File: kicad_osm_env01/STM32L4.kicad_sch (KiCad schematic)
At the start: 27 parts

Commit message: added stml433 to schematic and carried out some mods
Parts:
- added C? (x2): 100nF, Capacitor_SMD:C_0402_1005Metric, symbol device:C
- added C? (x2): 1uF, Capacitor_SMD:C_0402_1005Metric, symbol device:C
- added L?: 2A/0.05DCR, Inductor_SMD:L_0402_1005Metric, symbol device:Ferrite_Bead
- added R?: 0R, symbol device:R
- added U?: STM32L433VCTx, LQFP100, symbol Devtank:STM32L433VCTx
- C1, C12: value (none) -> 10pF; footprint (none) -> Capacitor_SMD:C_0402_1005Metric
- C13, C27: value (none) -> DNF; footprint (none) -> Capacitor_SMD:C_0402_1005Metric
- C28, C29, C30, C44, C51, C62: renamed from C?; value (none) -> 100nF; footprint (none) -> Capacitor_SMD:C_0402_1005Metric
- C59: renamed from C?; value (none) -> 4.7uF; footprint (none) -> Capacitor_SMD:C_0603_1608Metric
- C60: renamed from C?; value (none) -> 1uF; footprint (none) -> Capacitor_SMD:C_0402_1005Metric
- C61: renamed from C?; value (none) -> 10nF; footprint (none) -> Capacitor_SMD:C_0402_1005Metric
- D8: value (none) -> RED; footprint (none) -> Devtank_PCB_lib:LED_Rectangular_W4.5mm_H7.3mm_Horizontal_2.54mm_Z3.0mm
- J5: value (none) -> Conn_02x03_Odd_Even; footprint (none) -> Connector:Tag-Connect_TC2030-IDC-NL_2x03_P1.27mm_Vertical
- L2: renamed from L?; value (none) -> 2A/0.05DCR; footprint (none) -> Inductor_SMD:L_0402_1005Metric
- R119, R16: value (none) -> 10k; footprint (none) -> Resistor_SMD:R_0603_1608Metric
- R15, R30: value (none) -> DNF; footprint (none) -> Resistor_SMD:R_0603_1608Metric
- R26: value (none) -> 390R; footprint (none) -> Resistor_SMD:R_0603_1608Metric
- R37: value (none) -> 0R; footprint (none) -> Resistor_SMD:R_0603_1608Metric
- R6: value (none) -> 1.3k; footprint (none) -> Resistor_SMD:R_0603_1608Metric
- S1: value (none) -> B3U-1100P; footprint (none) -> Button_Switch_SMD:SW_SPST_B3U-1100P
- U14: value (none) -> STM32L451RCTx; footprint (none) -> Package_QFP:LQFP-64_10x10mm_P0.5mm
- Y1: value (none) -> 8MHZ; footprint (none) -> Crystal:Crystal_SMD_Abracon_ABM3C-4Pin_5.0x3.2mm
- Y2: value (none) -> DNF; footprint (none) -> Crystal:Crystal_SMD_7050-4Pin_7.0x5.0mm
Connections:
- net +3V3: now also C?.1, C?.1, L?.2, U?.100 (VDD), U?.11 (VDD), U?.28 (VDD), U?.50 (VDD), U?.73 (VDDUSB), U?.75 (VDD)
- net 32.768KHZ_crystal_out: now also U?.9 (ADC1_EXTI15/ADC2_EXTI15/ADC3_EXTI15/RCC_OSC32_OUT/PC15)
- net 3V3A_STM: now also U?.22 (VDDA)
- net 8MHZ_crystal_in: now also U?.12 (PH0/RCC_OSC_IN)
- net 8MHZ_crystal_out: now also U?.13 (PH1/RCC_OSC_OUT)
- net ADC2: now also U?.24 (ADC1_IN6/ADC2_IN6/LCD_SEG0/OPAMP1_VINM/TIM15_CH1N/TIM2_CH2/TIM5_CH2/UART4_RX/USART2_DE/USART2_RTS/PA1)
- net ADC3: now also U?.17 (ADC1_IN3/ADC2_IN3/ADC3_IN3/DFSDM_CKOUT/LCD_SEG20/LPTIM1_IN2/SPI2_MISO/PC2)
- net ADC4: now also U?.18 (ADC1_IN4/ADC2_IN4/ADC3_IN4/LCD_VLCD/LPTIM1_ETR/LPTIM2_ETR/SAI1_SD_A/SPI2_MOSI/PC3)
- net ADC5: now also U?.35 (ADC1_IN15/ADC2_IN15/COMP1_OUT/LCD_SEG5/OPAMP2_VOUT/QUADSPI_BK1_IO1/TIM1_CH2N/TIM3_CH3/TIM8_CH2N/USART3_CK/PB0)
- net ADC6: now also U?.36 (ADC1_IN16/ADC2_IN16/COMP1_INM/DFSDM_DATIN0/LCD_SEG6/LPTIM2_IN1/QUADSPI_BK1_IO0/TIM1_CH3N/TIM3_CH4/TIM8_CH3N/USART3_DE/USART3_RTS/PB1)
- net ADC7: now also U?.15 (ADC1_IN1/ADC2_IN1/ADC3_IN1/DFSDM_DATIN4/I2C3_SCL/LCD_SEG18/LPTIM1_IN1/LPTIM2_IN1/LPUART1_RX/PC0)
- net ADC8: now also U14.20 (ADC1_IN9/ADC2_IN9/DAC1_OUT1/LPTIM2_OUT/SAI1_FS_B/SPI1_NSS/SPI3_NSS/USART2_CK/PA4), U?.29 (ADC1_IN9/ADC2_IN9/DAC1_OUT1/LPTIM2_OUT/SAI1_FS_B/SPI1_NSS/SPI3_NSS/USART2_CK/PA4); no longer U14.9 (PC1/ADC1_IN2/ADC2_IN2/ADC3_IN2/DFSDM_CKIN4/I2C3_SDA/LCD_SEG19/LPTIM1_OUT/LPUART1_TX)
- net BOOT0: now also U?.94 (BOOT0)
- net CAN1_RX: now also U?.51 (DFSDM_DATIN1/I2C2_SMBA/LCD_SEG12/LPUART1_DE/LPUART1_RTS/SAI2_FS_A/SPI2_NSS/SWPMI1_IO/TIM15_BKIN/TIM1_BKIN/TIM1_BKIN_COMP2/TSC_G1_IO1/USART3_CK/PB12)
- net CAN1_TX: now also U?.52 (DFSDM_CKIN1/I2C2_SCL/LCD_SEG13/LPUART1_CTS/SAI2_SCK_A/SPI2_SCK/SWPMI1_TX/TIM15_CH1N/TIM1_CH1N/TSC_G1_IO2/USART3_CTS/PB13)
- net GND: now also C?.2, C?.2, C?.2, C?.2, U?.10 (VSS), U?.19 (VSSA), U?.20 (VREF-), U?.27 (VSS), U?.49 (VSS), U?.74 (VSS), U?.99 (VSS)
- net GPIO1: now also U?.63 (DFSDM_CKIN3/LCD_SEG24/SAI2_MCLK_A/SDMMC1_D6/TIM3_CH1/TIM8_CH1/TSC_G4_IO1/PC6)
- net GPIO10: now also U?.77 (ADC1_EXTI15/ADC2_EXTI15/ADC3_EXTI15/LCD_SEG17/SAI2_FS_B/SPI1_NSS/SPI3_NSS/SYS_JTDI/TIM2_CH1/TIM2_ETR/TSC_G3_IO1/UART4_DE/UART4_RTS/PA15)
- net GPIO11: now also U?.64 (DFSDM_DATIN3/LCD_SEG25/SAI2_MCLK_B/SDMMC1_D7/TIM3_CH2/TIM8_CH2/TSC_G4_IO2/PC7)
- net GPIO12: now also U?.90 (COMP2_INP/LCD_SEG8/SAI1_MCLK_B/SPI1_MISO/SPI3_MISO/SYS_JTRST/TIM17_BKIN/TIM3_CH1/TSC_G2_IO1/UART5_DE/UART5_RTS/USART1_CTS/PB4)
- net GPIO13: now also U?.91 (COMP2_OUT/I2C1_SMBA/LCD_SEG9/LPTIM1_IN1/SAI1_SD_B/SPI1_MOSI/SPI3_MOSI/TIM16_BKIN/TIM3_CH2/TSC_G2_IO2/UART5_CTS/USART1_CK/PB5)
- net GPIO14: now also U?.53 (DFSDM_DATIN2/I2C2_SDA/LCD_SEG14/SAI2_MCLK_A/SPI2_MISO/SWPMI1_RX/TIM15_CH1/TIM1_CH2N/TIM8_CH2N/TSC_G1_IO3/USART3_DE/USART3_RTS/PB14)
- net GPIO15: now also U?.54 (ADC1_EXTI15/ADC2_EXTI15/ADC3_EXTI15/DFSDM_CKIN2/LCD_SEG15/RTC_REFIN/SAI2_SD_A/SPI2_MOSI/SWPMI1_SUSPEND/TIM15_CH2/TIM1_CH3N/TIM8_CH3N/TSC_G1_IO4/PB15)
- net GPIO16: now also U?.83 (PD2/LCD_COM7/LCD_SEG31/LCD_SEG43/SDMMC1_CMD/TIM3_ETR/TSC_SYNC/UART5_RX/USART3_DE/USART3_RTS)
- net GPIO2: now also U?.65 (LCD_SEG26/SDMMC1_D0/TIM3_CH3/TIM8_CH3/TSC_G4_IO3/PC8)
- net GPIO3: now also U?.37 (COMP1_INP/DFSDM_CKIN0/I2C3_SMBA/LPTIM1_OUT/RTC_OUT_ALARM/RTC_OUT_CALIB/PB2)
- net GPIO4: now also U?.66 (DAC1_EXTI9/LCD_SEG27/SAI2_EXTCLK/SDMMC1_D1/TIM3_CH4/TIM8_BKIN2/TIM8_BKIN2_COMP1/TIM8_CH4/TSC_G4_IO4/USB_OTG_FS_NOE/PC9)
- net GPIO6: now also U?.89 (COMP2_INM/LCD_SEG7/SAI1_SCK_B/SPI1_SCK/SPI3_SCK/SYS_JTDO-SWO/TIM2_CH2/USART1_DE/USART1_RTS/PB3)
- net GPIO7: now also U?.80 (LCD_COM6/LCD_SEG30/LCD_SEG42/SAI2_SD_B/SDMMC1_CK/SPI3_MOSI/TSC_G3_IO4/UART5_TX/USART3_CK/PC12)
- net GPIO8: now also U?.70 (ADC1_EXTI11/ADC2_EXTI11/ADC3_EXTI11/CAN1_RX/TIM1_BKIN2/TIM1_BKIN2_COMP1/TIM1_CH4/USART1_CTS/USB_OTG_FS_DM/PA11)
- net GPIO9: now also U?.71 (CAN1_TX/TIM1_ETR/USART1_DE/USART1_RTS/USB_OTG_FS_DP/PA12)
- net I2C1_SCL: now also U?.95 (CAN1_RX/DFSDM_DATIN6/I2C1_SCL/LCD_SEG16/SAI1_MCLK_A/SDMMC1_D4/TIM16_CH1/TIM4_CH3/PB8)
- net I2C1_SDA: now also U?.96 (CAN1_TX/DAC1_EXTI9/DFSDM_CKIN6/I2C1_SDA/IR_OUT/LCD_COM3/SAI1_FS_A/SDMMC1_D5/SPI2_NSS/TIM17_CH1/TIM4_CH4/PB9)
- net LPUART1_RX: now also U?.47 (COMP1_OUT/DFSDM_DATIN7/I2C2_SCL/LCD_SEG10/LPUART1_RX/QUADSPI_CLK/SAI1_SCK_A/SPI2_SCK/TIM2_CH3/USART3_TX/PB10)
- net LPUART1_TX: now also U?.48 (ADC1_EXTI11/ADC2_EXTI11/ADC3_EXTI11/COMP2_OUT/DFSDM_CKIN7/I2C2_SDA/LCD_SEG11/LPUART1_TX/QUADSPI_NCS/TIM2_CH4/USART3_RX/PB11)
- net SAI1_FS_A: now also U?.68 (DAC1_EXTI9/LCD_COM1/TIM15_BKIN/TIM1_CH2/USART1_TX/USB_OTG_FS_VBUS/PA9)
- net SAI1_SCK_A: now also U?.67 (LCD_COM0/LPTIM2_OUT/RCC_MCO/TIM1_CH1/USART1_CK/USB_OTG_FS_SOF/PA8)
- net SAI1_SD_A: now also U?.69 (LCD_COM2/TIM17_BKIN/TIM1_CH3/USART1_RX/USB_OTG_FS_ID/PA10)
- net SPI1_CS: now also U14.9 (PC1/ADC1_IN2/ADC2_IN2/ADC3_IN2/DFSDM_CKIN4/I2C3_SDA/LCD_SEG19/LPTIM1_OUT/LPUART1_TX), U?.16 (ADC1_IN2/ADC2_IN2/ADC3_IN2/DFSDM_CKIN4/I2C3_SDA/LCD_SEG19/LPTIM1_OUT/LPUART1_TX/PC1); no longer U14.20 (ADC1_IN9/ADC2_IN9/DAC1_OUT1/LPTIM2_OUT/SAI1_FS_B/SPI1_NSS/SPI3_NSS/USART2_CK/PA4)
- net SPI1_MISO: now also U?.31 (ADC1_IN11/ADC2_IN11/LCD_SEG3/OPAMP2_VINP/QUADSPI_BK1_IO3/SPI1_MISO/TIM16_CH1/TIM1_BKIN/TIM1_BKIN_COMP2/TIM3_CH1/TIM8_BKIN/TIM8_BKIN_COMP2/USART3_CTS/PA6)
- net SPI1_MOSI: now also U?.32 (ADC1_IN12/ADC2_IN12/LCD_SEG4/OPAMP2_VINM/QUADSPI_BK1_IO2/SPI1_MOSI/TIM17_CH1/TIM1_CH1N/TIM3_CH2/TIM8_CH1N/PA7)
- net SPI1_SCK: now also U?.30 (ADC1_IN10/ADC2_IN10/DAC1_OUT2/LPTIM2_ETR/SPI1_SCK/TIM2_CH1/TIM2_ETR/TIM8_CH1N/PA5)
- net STM_NRST: now also U?.14 (NRST)
- net SWCLK: now also U?.76 (SYS_JTCK-SWCLK/PA14)
- net SWD_IO: now also U?.72 (IR_OUT/SYS_JTMS-SWDIO/USB_OTG_FS_NOE/PA13)
- net UART4_RX: now also U?.79 (ADC1_EXTI11/ADC2_EXTI11/ADC3_EXTI11/LCD_COM5/LCD_SEG29/LCD_SEG41/SAI2_MCLK_B/SDMMC1_D3/SPI3_MISO/TSC_G3_IO3/UART4_RX/USART3_RX/PC11)
- net UART4_TX: now also U?.78 (LCD_COM4/LCD_SEG28/LCD_SEG40/SAI2_SCK_B/SDMMC1_D2/SPI3_SCK/TSC_G3_IO2/UART4_TX/USART3_TX/PC10)
- net USART1_RX: now also U?.93 (COMP2_INM/DFSDM_CKIN5/FMC_NL/I2C1_SDA/LCD_SEG21/LPTIM1_IN2/SYS_PVD_IN/TIM17_CH1N/TIM4_CH2/TIM8_BKIN/TIM8_BKIN_COMP1/TSC_G2_IO4/UART4_CTS/USART1_RX/PB7)
- net USART1_TX: now also U?.92 (COMP2_INP/DFSDM_DATIN5/I2C1_SCL/LPTIM1_ETR/SAI1_FS_B/TIM16_CH1N/TIM4_CH1/TIM8_BKIN2/TIM8_BKIN2_COMP2/TSC_G2_IO3/USART1_TX/PB6)
- net USART2_RX: now also U?.26 (ADC1_IN8/ADC2_IN8/LCD_SEG2/OPAMP1_VOUT/TIM15_CH2/TIM2_CH4/TIM5_CH4/USART2_RX/PA3)
- net USART2_TX: now also U?.25 (ADC1_IN7/ADC2_IN7/LCD_SEG1/RCC_LSCO/SAI2_EXTCLK/SYS_WKUP4/TIM15_CH1/TIM2_CH3/TIM5_CH3/USART2_TX/PA2)
- net USART3_RX: now also U?.34 (ADC1_IN14/ADC2_IN14/COMP1_INP/LCD_SEG23/SYS_WKUP5/USART3_RX/PC5)
- net USART3_TX: now also U?.33 (ADC1_IN13/ADC2_IN13/COMP1_INM/LCD_SEG22/USART3_TX/PC4)
- net WKUP2: now also U?.7 (RTC_OUT_ALARM/RTC_OUT_CALIB/RTC_TAMP1/RTC_TS/SYS_WKUP2/PC13)
- net status_led: now also U?.23 (ADC1_IN5/ADC2_IN5/OPAMP1_VINP/RTC_TAMP2/SAI1_EXTCLK/SYS_WKUP1/TIM2_CH1/TIM2_ETR/TIM5_CH1/TIM8_ETR/UART4_TX/USART2_CTS/PA0)
- net VBAT: now reaches R37.1, U14.1 (VBAT)
- net VBAT: now also U?.6 (VBAT)
- new net: R?.2, U?.21 (VREF+/VREFBUF_OUT)
- new net VREF+: C?.1, C?.1, L?.1, R?.1
- no-connect marks 3 -> 34
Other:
- note added: "VDDUSB"
- moved on the sheet: C1, C12, C13, C27, C28, C29, C30, C44, C51, C59, C60, C61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

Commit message: updated mod list
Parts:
- removed R37: 0R, Resistor_SMD:R_0603_1608Metric, symbol device:R
- added D? (x3): RB160M-40TR, Diode_SMD:D_SOD-123, symbol OSM_env01-rescue:D_Schottky-device-ESP32-EVB_Rev_D-rescue
- added J?: Conn_02x03_Odd_Even, Connector:Tag-Connect_TC2030-IDC-NL_2x03_P1.27mm_Vertical, symbol Connector:Conn_02x03_Odd_Even
- added R? (x5): 0R, symbol device:R
- added R? (x2): DNF, symbol device:R
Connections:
- net UART4_RX is gone; now on net LPUART1_RX: U14.52 (PC11/ADC1_EXTI11/ADC2_EXTI11/ADC3_EXTI11/LCD_COM5/LCD_SEG29/LCD_SEG41/SAI2_MCLK_B/SDMMC1_D3/SPI3_MISO/TSC_G3_IO3/UART4_RX/USART3_RX), U?.79 (ADC1_EXTI11/ADC2_EXTI11/ADC3_EXTI11/LCD_COM5/LCD_SEG29/LCD_SEG41/SAI2_MCLK_B/SDMMC1_D3/SPI3_MISO/TSC_G3_IO3/UART4_RX/USART3_RX/PC11)
- net UART4_TX is gone; now on net LPUART1_TX: U14.51 (PC10/LCD_COM4/LCD_SEG28/LCD_SEG40/SAI2_SCK_B/SDMMC1_D2/SPI3_SCK/TSC_G3_IO2/UART4_TX/USART3_TX), U?.78 (LCD_COM4/LCD_SEG28/LCD_SEG40/SAI2_SCK_B/SDMMC1_D2/SPI3_SCK/TSC_G3_IO2/UART4_TX/USART3_TX/PC10)
- net +3V3: now also D?.2 (A), J?.1 (Pin_1), R?.1; no longer C51.2, U?.73 (VDDUSB)
- net 32.768KHZ_crystal_in: now also U?.8 (RCC_OSC32_IN/PC14)
- net CAN1_RX: now also R?.2, R?.2, R?.2; no longer U14.33 (DFSDM_DATIN1/I2C2_SMBA/LCD_SEG12/LPUART1_DE/LPUART1_RTS/SAI2_FS_A/SPI2_NSS/SWPMI1_IO/TIM15_BKIN/TIM1_BKIN/TIM1_BKIN_COMP2/TSC_G1_IO1/USART3_CK/PB12), U?.51 (DFSDM_DATIN1/I2C2_SMBA/LCD_SEG12/LPUART1_DE/LPUART1_RTS/SAI2_FS_A/SPI2_NSS/SWPMI1_IO/TIM15_BKIN/TIM1_BKIN/TIM1_BKIN_COMP2/TSC_G1_IO1/USART3_CK/PB12)
- net CAN1_TX: now also R?.2, R?.2, R?.2; no longer U14.34 (DFSDM_CKIN1/I2C2_SCL/LCD_SEG13/LPUART1_CTS/SAI2_SCK_A/SPI2_SCK/SWPMI1_TX/TIM15_CH1N/TIM1_CH1N/TSC_G1_IO2/USART3_CTS/PB13), U?.52 (DFSDM_CKIN1/I2C2_SCL/LCD_SEG13/LPUART1_CTS/SAI2_SCK_A/SPI2_SCK/SWPMI1_TX/TIM15_CH1N/TIM1_CH1N/TSC_G1_IO2/USART3_CTS/PB13)
- net GND: now also J?.2 (Pin_2)
- net GPIO12: now also U14.35 (DFSDM_DATIN2/I2C2_SDA/LCD_SEG14/SAI2_MCLK_A/SPI2_MISO/SWPMI1_RX/TIM15_CH1/TIM1_CH2N/TIM8_CH2N/TSC_G1_IO3/USART3_DE/USART3_RTS/PB14), U?.53 (DFSDM_DATIN2/I2C2_SDA/LCD_SEG14/SAI2_MCLK_A/SPI2_MISO/SWPMI1_RX/TIM15_CH1/TIM1_CH2N/TIM8_CH2N/TSC_G1_IO3/USART3_DE/USART3_RTS/PB14); no longer U14.56 (COMP2_INP/LCD_SEG8/SAI1_MCLK_B/SPI1_MISO/SPI3_MISO/SYS_JTRST/TIM17_BKIN/TIM3_CH1/TSC_G2_IO1/UART5_DE/UART5_RTS/USART1_CTS/PB4), U?.90 (COMP2_INP/LCD_SEG8/SAI1_MCLK_B/SPI1_MISO/SPI3_MISO/SYS_JTRST/TIM17_BKIN/TIM3_CH1/TSC_G2_IO1/UART5_DE/UART5_RTS/USART1_CTS/PB4)
- net GPIO13: now also U14.36 (ADC1_EXTI15/ADC2_EXTI15/ADC3_EXTI15/DFSDM_CKIN2/LCD_SEG15/RTC_REFIN/SAI2_SD_A/SPI2_MOSI/SWPMI1_SUSPEND/TIM15_CH2/TIM1_CH3N/TIM8_CH3N/TSC_G1_IO4/PB15), U?.54 (ADC1_EXTI15/ADC2_EXTI15/ADC3_EXTI15/DFSDM_CKIN2/LCD_SEG15/RTC_REFIN/SAI2_SD_A/SPI2_MOSI/SWPMI1_SUSPEND/TIM15_CH2/TIM1_CH3N/TIM8_CH3N/TSC_G1_IO4/PB15); no longer U14.57 (COMP2_OUT/I2C1_SMBA/LCD_SEG9/LPTIM1_IN1/SAI1_SD_B/SPI1_MOSI/SPI3_MOSI/TIM16_BKIN/TIM3_CH2/TSC_G2_IO2/UART5_CTS/USART1_CK/PB5), U?.91 (COMP2_OUT/I2C1_SMBA/LCD_SEG9/LPTIM1_IN1/SAI1_SD_B/SPI1_MOSI/SPI3_MOSI/TIM16_BKIN/TIM3_CH2/TSC_G2_IO2/UART5_CTS/USART1_CK/PB5)
- net GPIO14: now also U14.54 (PD2/LCD_COM7/LCD_SEG31/LCD_SEG43/SDMMC1_CMD/TIM3_ETR/TSC_SYNC/UART5_RX/USART3_DE/USART3_RTS), U?.83 (PD2/LCD_COM7/LCD_SEG31/LCD_SEG43/SDMMC1_CMD/TIM3_ETR/TSC_SYNC/UART5_RX/USART3_DE/USART3_RTS); no longer U14.35 (DFSDM_DATIN2/I2C2_SDA/LCD_SEG14/SAI2_MCLK_A/SPI2_MISO/SWPMI1_RX/TIM15_CH1/TIM1_CH2N/TIM8_CH2N/TSC_G1_IO3/USART3_DE/USART3_RTS/PB14), U?.53 (DFSDM_DATIN2/I2C2_SDA/LCD_SEG14/SAI2_MCLK_A/SPI2_MISO/SWPMI1_RX/TIM15_CH1/TIM1_CH2N/TIM8_CH2N/TSC_G1_IO3/USART3_DE/USART3_RTS/PB14)
- net GPIO15: now also U14.29 (COMP1_OUT/DFSDM_DATIN7/I2C2_SCL/LCD_SEG10/LPUART1_RX/QUADSPI_CLK/SAI1_SCK_A/SPI2_SCK/TIM2_CH3/USART3_TX/PB10), U?.47 (COMP1_OUT/DFSDM_DATIN7/I2C2_SCL/LCD_SEG10/LPUART1_RX/QUADSPI_CLK/SAI1_SCK_A/SPI2_SCK/TIM2_CH3/USART3_TX/PB10); no longer U14.36 (ADC1_EXTI15/ADC2_EXTI15/ADC3_EXTI15/DFSDM_CKIN2/LCD_SEG15/RTC_REFIN/SAI2_SD_A/SPI2_MOSI/SWPMI1_SUSPEND/TIM15_CH2/TIM1_CH3N/TIM8_CH3N/TSC_G1_IO4/PB15), U?.54 (ADC1_EXTI15/ADC2_EXTI15/ADC3_EXTI15/DFSDM_CKIN2/LCD_SEG15/RTC_REFIN/SAI2_SD_A/SPI2_MOSI/SWPMI1_SUSPEND/TIM15_CH2/TIM1_CH3N/TIM8_CH3N/TSC_G1_IO4/PB15)
- net GPIO16: now also U14.30 (ADC1_EXTI11/ADC2_EXTI11/ADC3_EXTI11/COMP2_OUT/DFSDM_CKIN7/I2C2_SDA/LCD_SEG11/LPUART1_TX/QUADSPI_NCS/TIM2_CH4/USART3_RX/PB11), U?.48 (ADC1_EXTI11/ADC2_EXTI11/ADC3_EXTI11/COMP2_OUT/DFSDM_CKIN7/I2C2_SDA/LCD_SEG11/LPUART1_TX/QUADSPI_NCS/TIM2_CH4/USART3_RX/PB11); no longer U14.54 (PD2/LCD_COM7/LCD_SEG31/LCD_SEG43/SDMMC1_CMD/TIM3_ETR/TSC_SYNC/UART5_RX/USART3_DE/USART3_RTS), U?.83 (PD2/LCD_COM7/LCD_SEG31/LCD_SEG43/SDMMC1_CMD/TIM3_ETR/TSC_SYNC/UART5_RX/USART3_DE/USART3_RTS)
- net GPIO8: now also U14.56 (COMP2_INP/LCD_SEG8/SAI1_MCLK_B/SPI1_MISO/SPI3_MISO/SYS_JTRST/TIM17_BKIN/TIM3_CH1/TSC_G2_IO1/UART5_DE/UART5_RTS/USART1_CTS/PB4), U?.90 (COMP2_INP/LCD_SEG8/SAI1_MCLK_B/SPI1_MISO/SPI3_MISO/SYS_JTRST/TIM17_BKIN/TIM3_CH1/TSC_G2_IO1/UART5_DE/UART5_RTS/USART1_CTS/PB4); no longer U14.44 (ADC1_EXTI11/ADC2_EXTI11/ADC3_EXTI11/CAN1_RX/TIM1_BKIN2/TIM1_BKIN2_COMP1/TIM1_CH4/USART1_CTS/USB_OTG_FS_DM/PA11), U?.70 (ADC1_EXTI11/ADC2_EXTI11/ADC3_EXTI11/CAN1_RX/TIM1_BKIN2/TIM1_BKIN2_COMP1/TIM1_CH4/USART1_CTS/USB_OTG_FS_DM/PA11)
- net GPIO9: now also U14.57 (COMP2_OUT/I2C1_SMBA/LCD_SEG9/LPTIM1_IN1/SAI1_SD_B/SPI1_MOSI/SPI3_MOSI/TIM16_BKIN/TIM3_CH2/TSC_G2_IO2/UART5_CTS/USART1_CK/PB5), U?.91 (COMP2_OUT/I2C1_SMBA/LCD_SEG9/LPTIM1_IN1/SAI1_SD_B/SPI1_MOSI/SPI3_MOSI/TIM16_BKIN/TIM3_CH2/TSC_G2_IO2/UART5_CTS/USART1_CK/PB5); no longer U14.45 (CAN1_TX/TIM1_ETR/USART1_DE/USART1_RTS/USB_OTG_FS_DP/PA12), U?.71 (CAN1_TX/TIM1_ETR/USART1_DE/USART1_RTS/USB_OTG_FS_DP/PA12)
- net LPUART1_RX: no longer U14.29 (COMP1_OUT/DFSDM_DATIN7/I2C2_SCL/LCD_SEG10/LPUART1_RX/QUADSPI_CLK/SAI1_SCK_A/SPI2_SCK/TIM2_CH3/USART3_TX/PB10), U?.47 (COMP1_OUT/DFSDM_DATIN7/I2C2_SCL/LCD_SEG10/LPUART1_RX/QUADSPI_CLK/SAI1_SCK_A/SPI2_SCK/TIM2_CH3/USART3_TX/PB10)
- net LPUART1_TX: no longer U14.30 (ADC1_EXTI11/ADC2_EXTI11/ADC3_EXTI11/COMP2_OUT/DFSDM_CKIN7/I2C2_SDA/LCD_SEG11/LPUART1_TX/QUADSPI_NCS/TIM2_CH4/USART3_RX/PB11), U?.48 (ADC1_EXTI11/ADC2_EXTI11/ADC3_EXTI11/COMP2_OUT/DFSDM_CKIN7/I2C2_SDA/LCD_SEG11/LPUART1_TX/QUADSPI_NCS/TIM2_CH4/USART3_RX/PB11)
- net STM_NRST: now also J?.5 (Pin_5)
- net SWCLK: now also J?.4 (Pin_4)
- net SWD_IO: now also J?.6 (Pin_6)
- net VBAT: now also C51.2, D?.1 (K), D?.1 (K), D?.1 (K), D?.2 (A)
- new net: R?.1, U14.44 (ADC1_EXTI11/ADC2_EXTI11/ADC3_EXTI11/CAN1_RX/TIM1_BKIN2/TIM1_BKIN2_COMP1/TIM1_CH4/USART1_CTS/USB_OTG_FS_DM/PA11)
- new net: R?.1, U14.45 (CAN1_TX/TIM1_ETR/USART1_DE/USART1_RTS/USB_OTG_FS_DP/PA12)
- new net: R?.1, U?.70 (ADC1_EXTI11/ADC2_EXTI11/ADC3_EXTI11/CAN1_RX/TIM1_BKIN2/TIM1_BKIN2_COMP1/TIM1_CH4/USART1_CTS/USB_OTG_FS_DM/PA11)
- new net: R?.1, U?.71 (CAN1_TX/TIM1_ETR/USART1_DE/USART1_RTS/USB_OTG_FS_DP/PA12)
- new net: R?.2, U?.73 (VDDUSB)
- new net +VBAT: D?.2 (A)
- new net PB12: R?.1, U14.33 (DFSDM_DATIN1/I2C2_SMBA/LCD_SEG12/LPUART1_DE/LPUART1_RTS/SAI2_FS_A/SPI2_NSS/SWPMI1_IO/TIM15_BKIN/TIM1_BKIN/TIM1_BKIN_COMP2/TSC_G1_IO1/USART3_CK/PB12), U?.51 (DFSDM_DATIN1/I2C2_SMBA/LCD_SEG12/LPUART1_DE/LPUART1_RTS/SAI2_FS_A/SPI2_NSS/SWPMI1_IO/TIM15_BKIN/TIM1_BKIN/TIM1_BKIN_COMP2/TSC_G1_IO1/USART3_CK/PB12)
- new net PB13: R?.1, U14.34 (DFSDM_CKIN1/I2C2_SCL/LCD_SEG13/LPUART1_CTS/SAI2_SCK_A/SPI2_SCK/SWPMI1_TX/TIM15_CH1N/TIM1_CH1N/TSC_G1_IO2/USART3_CTS/PB13), U?.52 (DFSDM_CKIN1/I2C2_SCL/LCD_SEG13/LPUART1_CTS/SAI2_SCK_A/SPI2_SCK/SWPMI1_TX/TIM15_CH1N/TIM1_CH1N/TSC_G1_IO2/USART3_CTS/PB13)
- no-connect marks 34 -> 35
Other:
- note added: "SWD Programming Header direct connect"
- note added: "SWD Programming Header tag connect"
- note added: "please not usb may not be available on all packages"
- note removed: "SWD Programming Header"
- moved on the sheet: C51

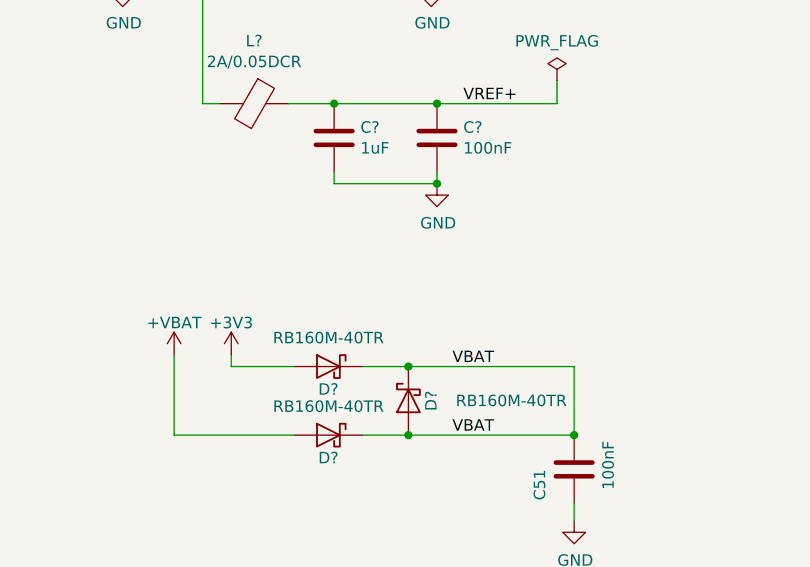
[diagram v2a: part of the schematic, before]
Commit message: updated schematics
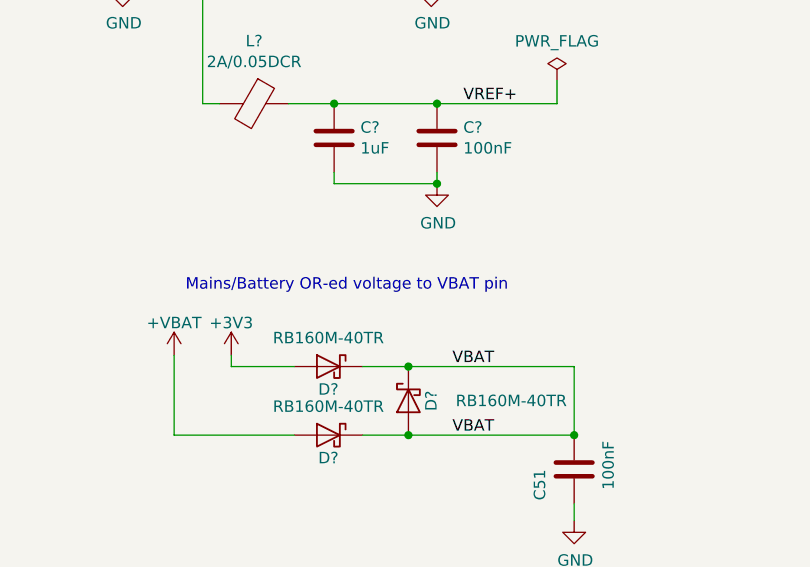
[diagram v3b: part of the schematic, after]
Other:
- note added: "Mains/Battery OR-ed voltage to VBAT pin"
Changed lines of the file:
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@@
+    (effects (font (size 1.27 1.27)) (justify left bottom))
+  )
+  (text "Mains/Battery OR-ed voltage to VBAT pin " (at 81.915 75.565 0)
     (effects (font (size 1.27 1.27)) (justify left bottom))
   )

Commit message: added new battery charge ic u2
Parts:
- removed J5: Conn_02x03_Odd_Even, Connector:Tag-Connect_TC2030-IDC-NL_2x03_P1.27mm_Vertical, symbol Connector:Conn_02x03_Odd_Even
- removed R? (x2): 0R, symbol device:R
- removed R? (x2): DNF, symbol device:R
- removed U14: STM32L451RCTx, Package_QFP:LQFP-64_10x10mm_P0.5mm, symbol Devtank:STM32L451RCTx
- gave numbers to parts that had none: 14
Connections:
- net BOOT0 renamed STM_BOOT0
- no-connect marks 35 -> 34
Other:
- note added: "STM32l451 Note: For comfirmation of pin functions refer to datasheet. Symbol may not be correct - wkup pins 2,14,16,25 -pa13, pa15, pb4 avoid as after reset internal pull up and pull down activated"
- note removed: "Note: For comfirmation of pin functions refer to datasheet. Symbol may not be correct - wkup pins 2,14,16,25 -pa13, pa15, pb4 avoid as after reset internal pull up and pull down activated"
- note removed: "SWD Programming Header tag connect"
- moved on the sheet: C1, C12, C13, C27, C62, D8, J6, R119, R12, R13, R14, R15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

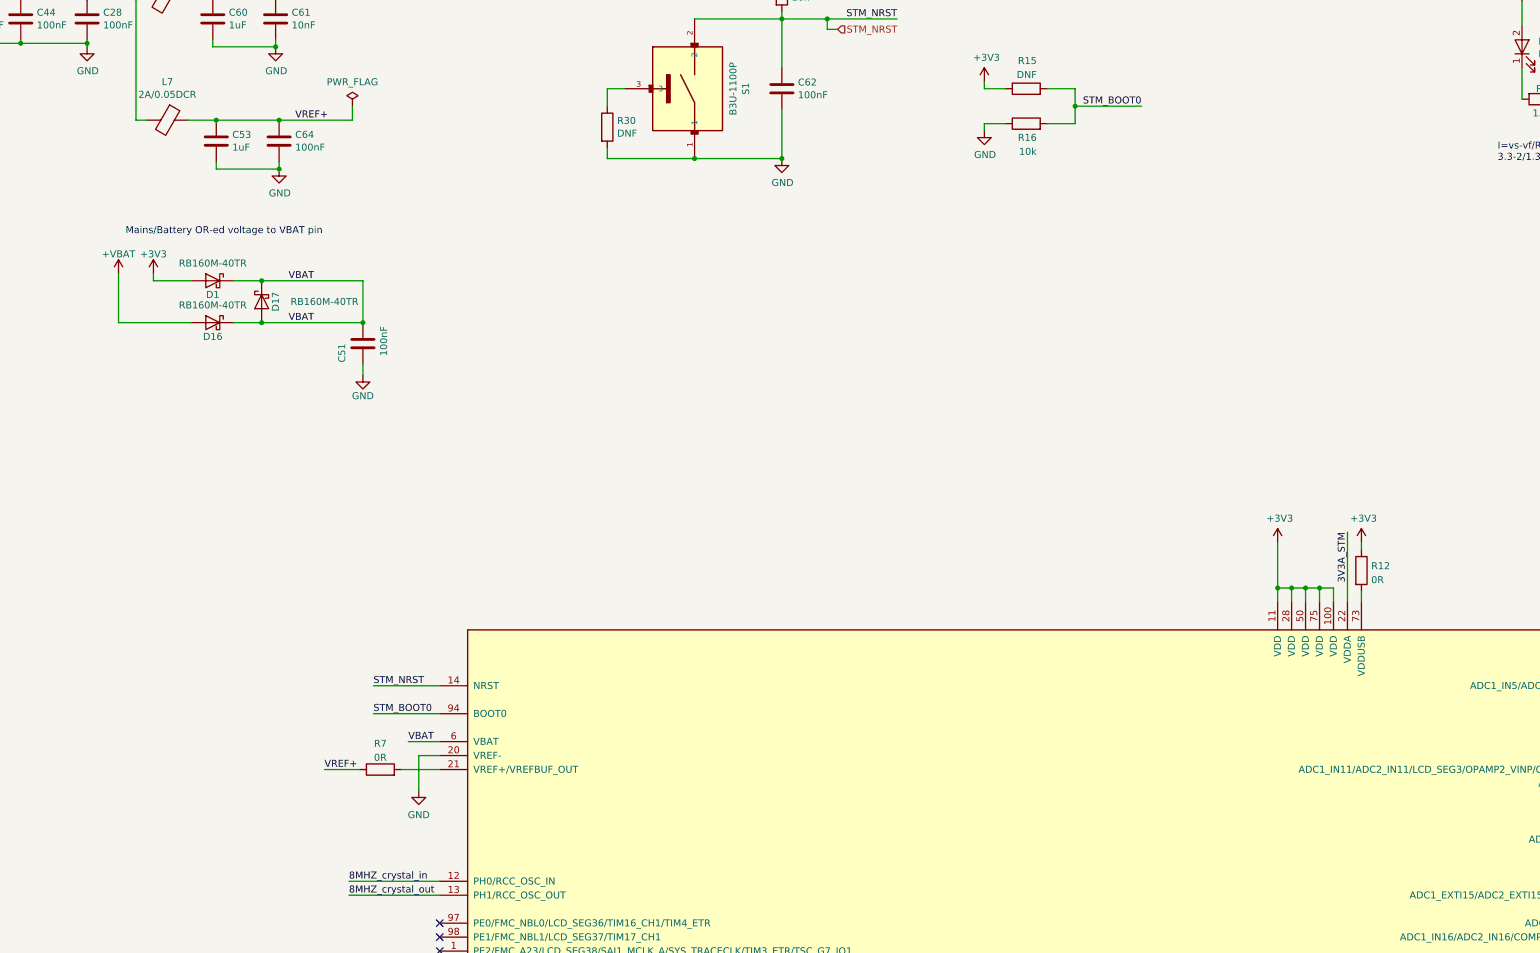
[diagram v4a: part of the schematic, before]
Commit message: updated schematics and added rs232
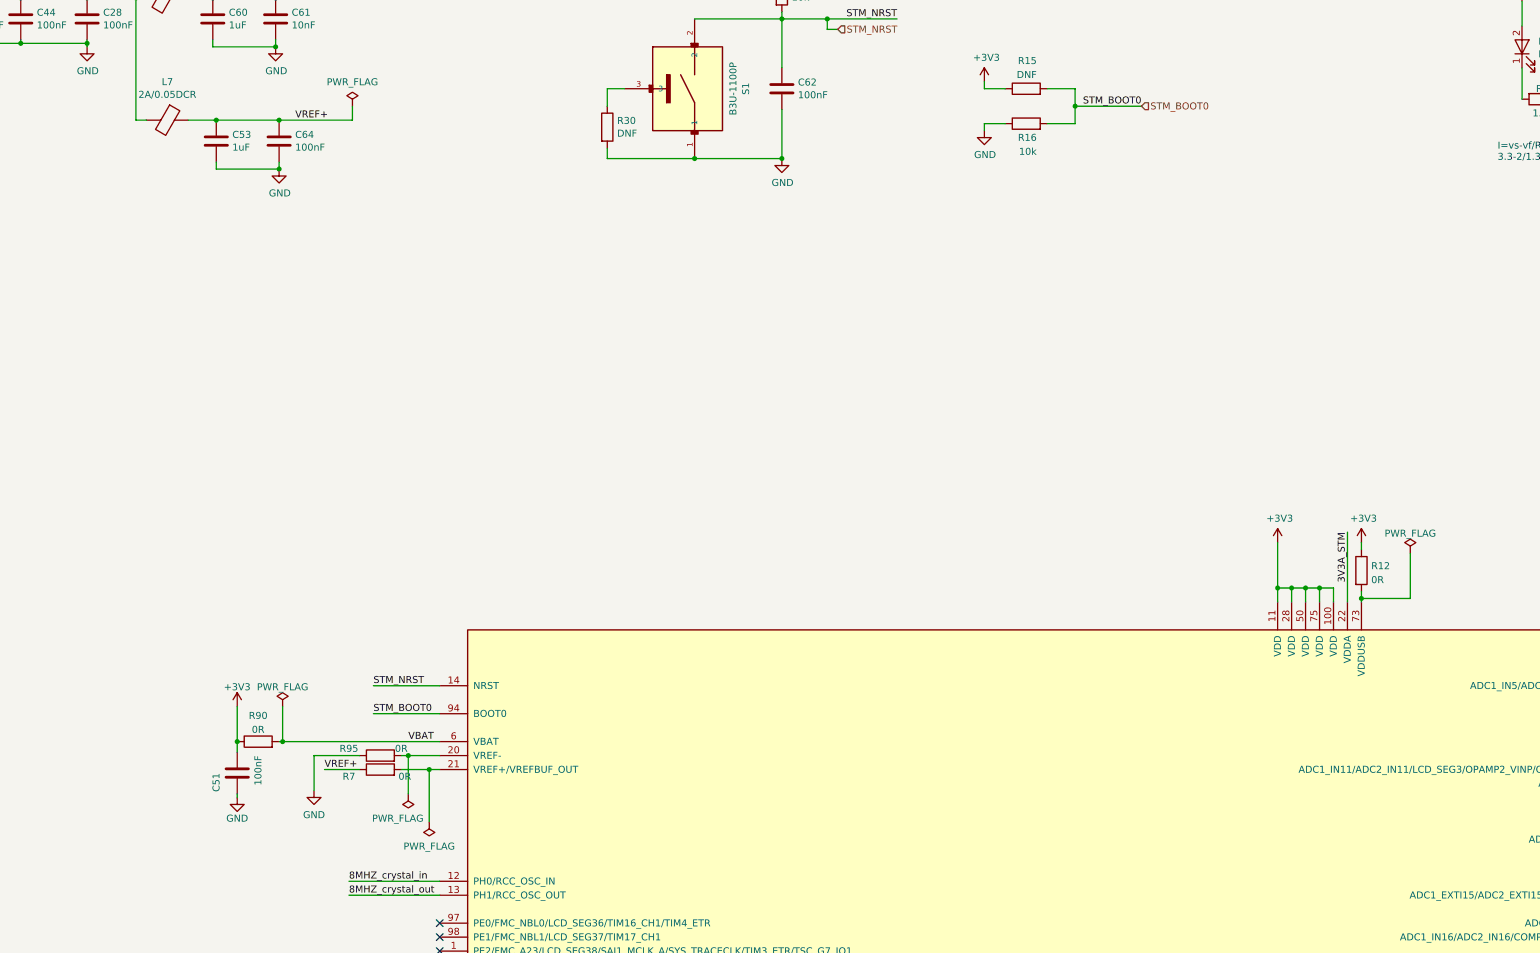
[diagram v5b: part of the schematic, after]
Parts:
- removed D1, D16, D17: RB160M-40TR, Diode_SMD:D_SOD-123, symbol OSM_env01-rescue:D_Schottky-device-ESP32-EVB_Rev_D-rescue
- added R90, R95: 0R, symbol Device:R
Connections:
- net +3V3: now also C51.2, R90.1
- net GND: now also R95.1; no longer U6.20 (VREF-)
- net VBAT: now also R90.2; no longer C51.2
- new net: R95.2, U6.20 (VREF-)
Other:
- note removed: "Mains/Battery OR-ed voltage to VBAT pin"
- moved on the sheet: C51
